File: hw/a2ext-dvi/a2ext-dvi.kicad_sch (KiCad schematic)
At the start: 11 parts, among them J1 Carrier IDC20, J2 HDMI-SWM-19 / Type A

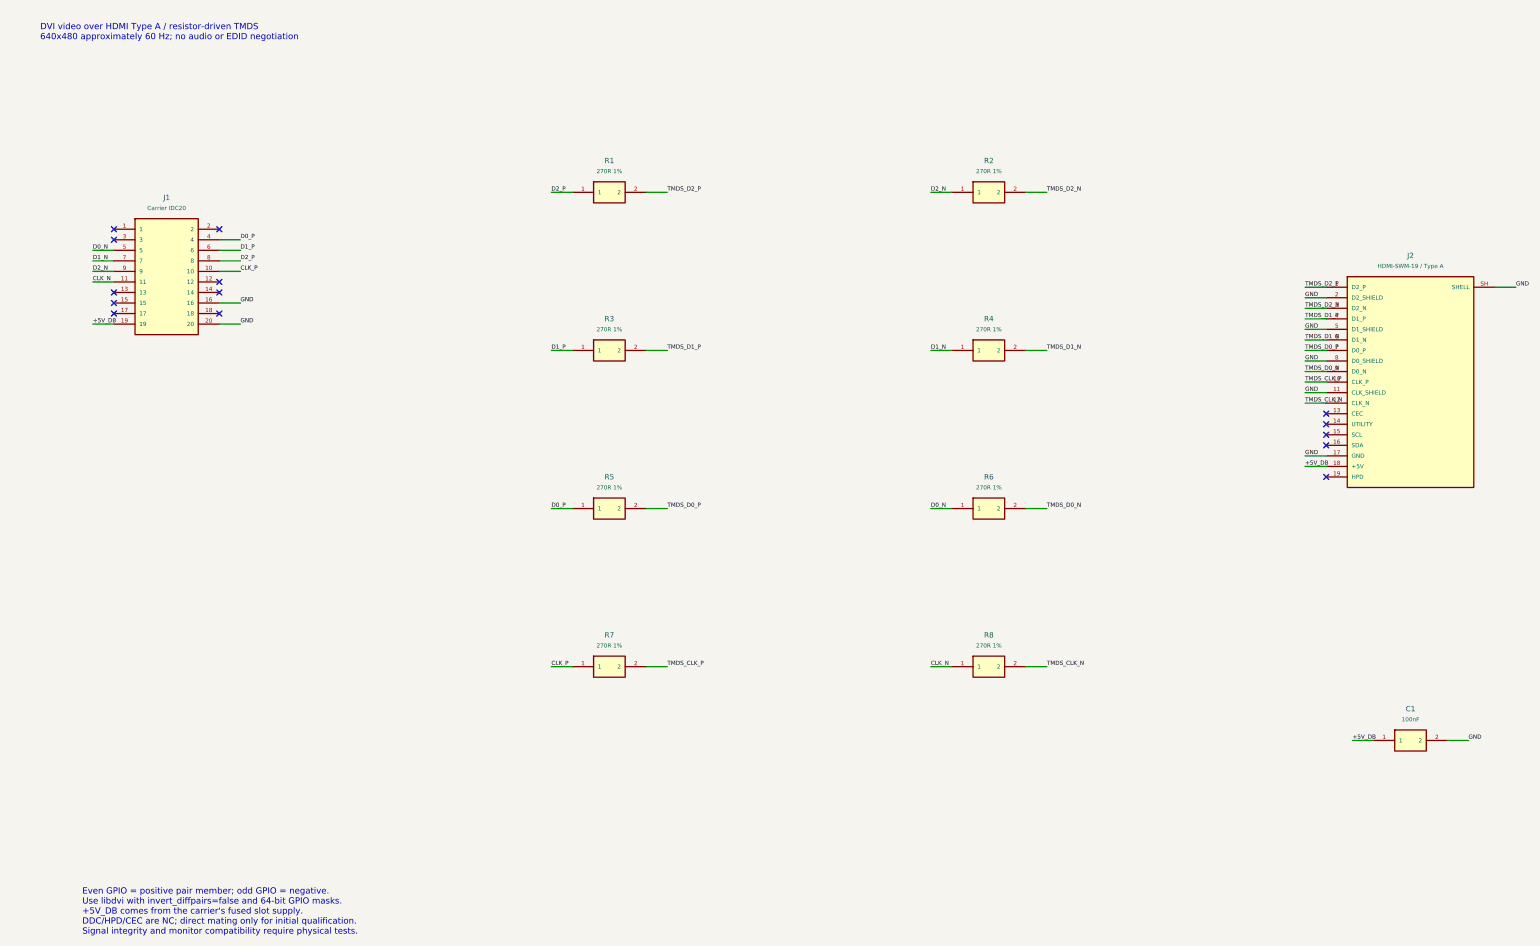
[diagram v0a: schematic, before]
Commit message: Simplify carrier to direct bus and slot power; improve schematic readability
Remove bus isolation and USB power circuitry, clarify signal labels, and reflow all schematics onto A4 landscape with larger text. Update PDFs, BOMs, connectivity checks, operating documentation, progress, and remaining tasks.
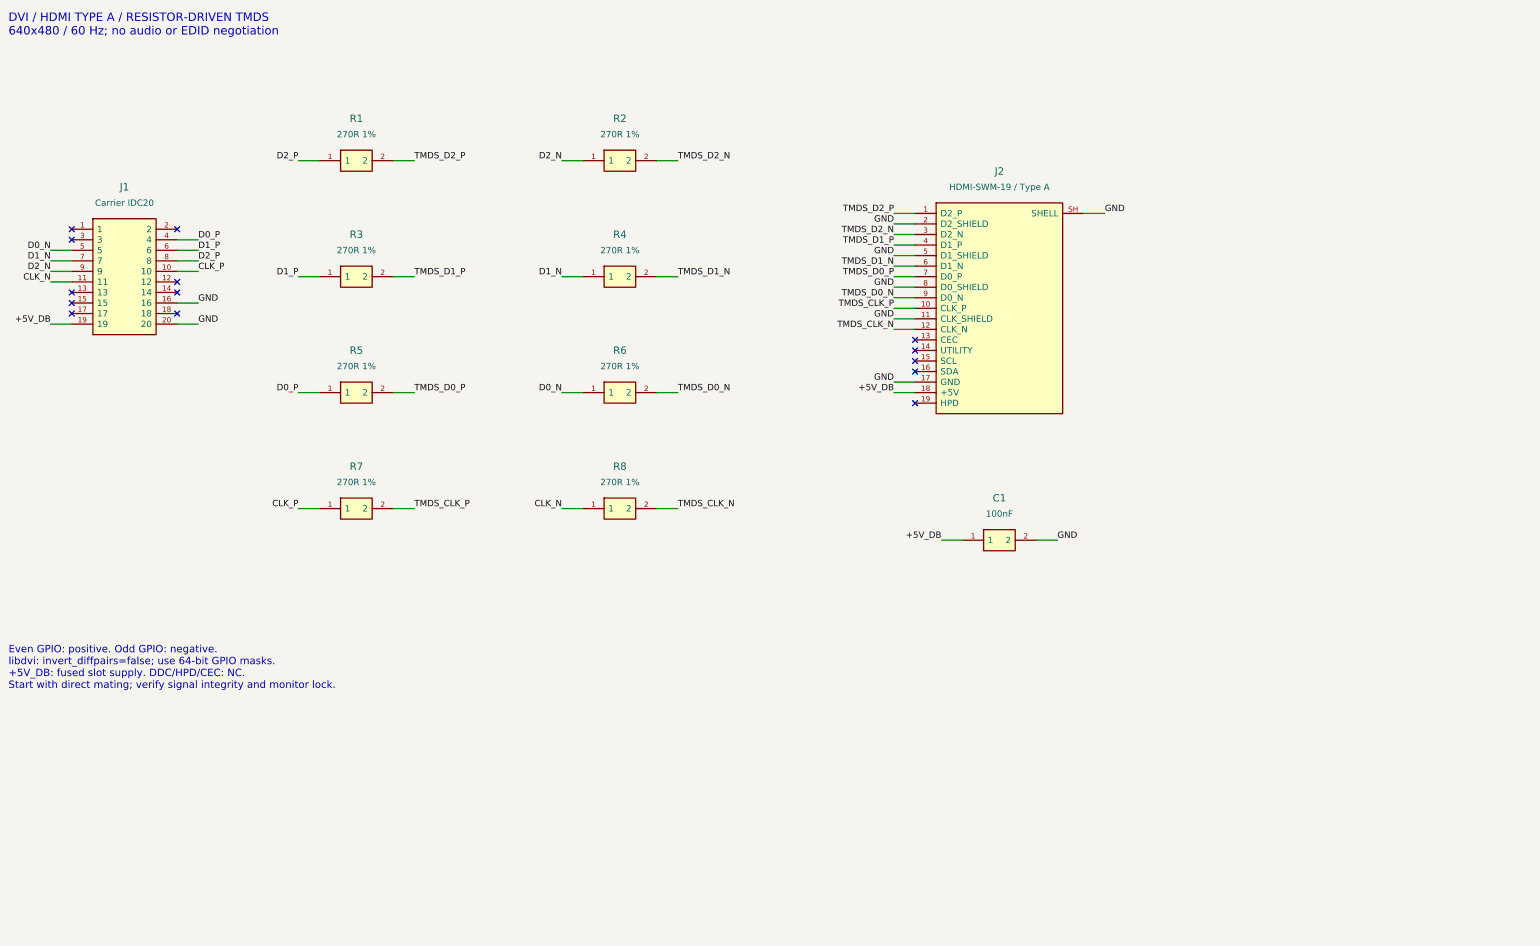
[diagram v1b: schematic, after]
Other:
- note added: "DVI / HDMI TYPE A / RESISTOR-DRIVEN TMDS 640x480 / 60 Hz; no audio or EDID negotiation"
- note added: "Even GPIO: positive. Odd GPIO: negative. libdvi: invert_diffpairs=false; use 64-bit GPIO masks. +5V_DB: fused slot supply. DDC/HPD/CEC: NC. Start with direct mating; verify signal integrity and monitor lock."
- note removed: "DVI video over HDMI Type A / resistor-driven TMDS 640x480 approximately 60 Hz; no audio or EDID negotiation"
- note removed: "Even GPIO = positive pair member; odd GPIO = negative. Use libdvi with invert_diffpairs=false and 64-bit GPIO masks. +5V_DB comes from the carrier's fused slot supply. DDC/HPD/CEC are NC; direct mating only for initial qualification. Signal integrity and monitor compatibility require physical tests."
- moved on the sheet: C1, J1, J2, R1, R2, R3, R4, R5, R6, R7, R8

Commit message: Add two-layer prototype PCBs and Gerber packages for all boards
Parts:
- C1: footprint (none) -> A2Ext:C0805
- J1: footprint (none) -> A2Ext:Socket20
- J2: footprint (none) -> A2Ext:HDMI_Molex
- R1, R2, R3, R4, R5, R6, R7, R8: footprint (none) -> A2Ext:R0402

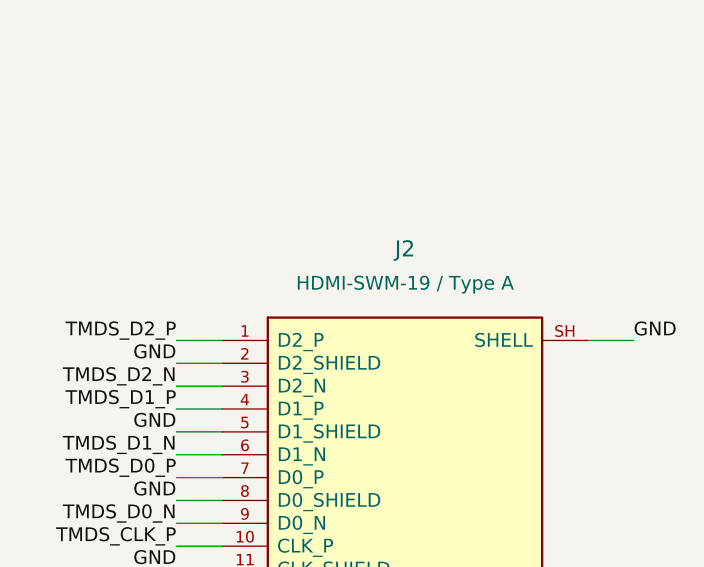
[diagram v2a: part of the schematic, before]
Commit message: Revise all prototype PCBs for through-hole assembly
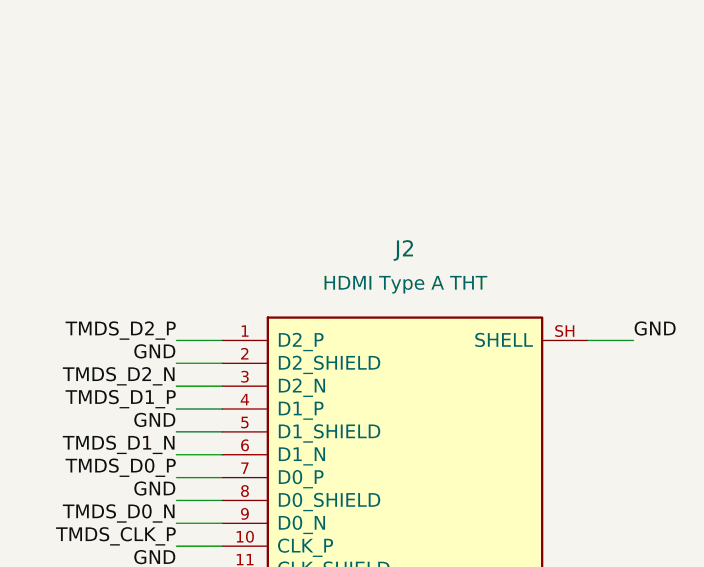
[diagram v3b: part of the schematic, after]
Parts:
- C1: footprint A2Ext:C0805 -> A2Ext:C_Radial_5
- J2: value HDMI-SWM-19 / Type A -> HDMI Type A THT; footprint A2Ext:HDMI_Molex -> A2Ext:HDMI_Kycon_THT
- R1, R2, R3, R4, R5, R6, R7, R8: footprint A2Ext:R0402 -> A2Ext:R_Axial_7.62
